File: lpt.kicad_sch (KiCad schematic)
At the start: 25 parts, among them J6 DB25 FEMALE, K1 TE_OJS_5V_10A, Q3 BC857, U2 74HC245, U3 74HC245, U4 LM358EDR2G, U5 ACSL-6400, U7 ACSL-6400

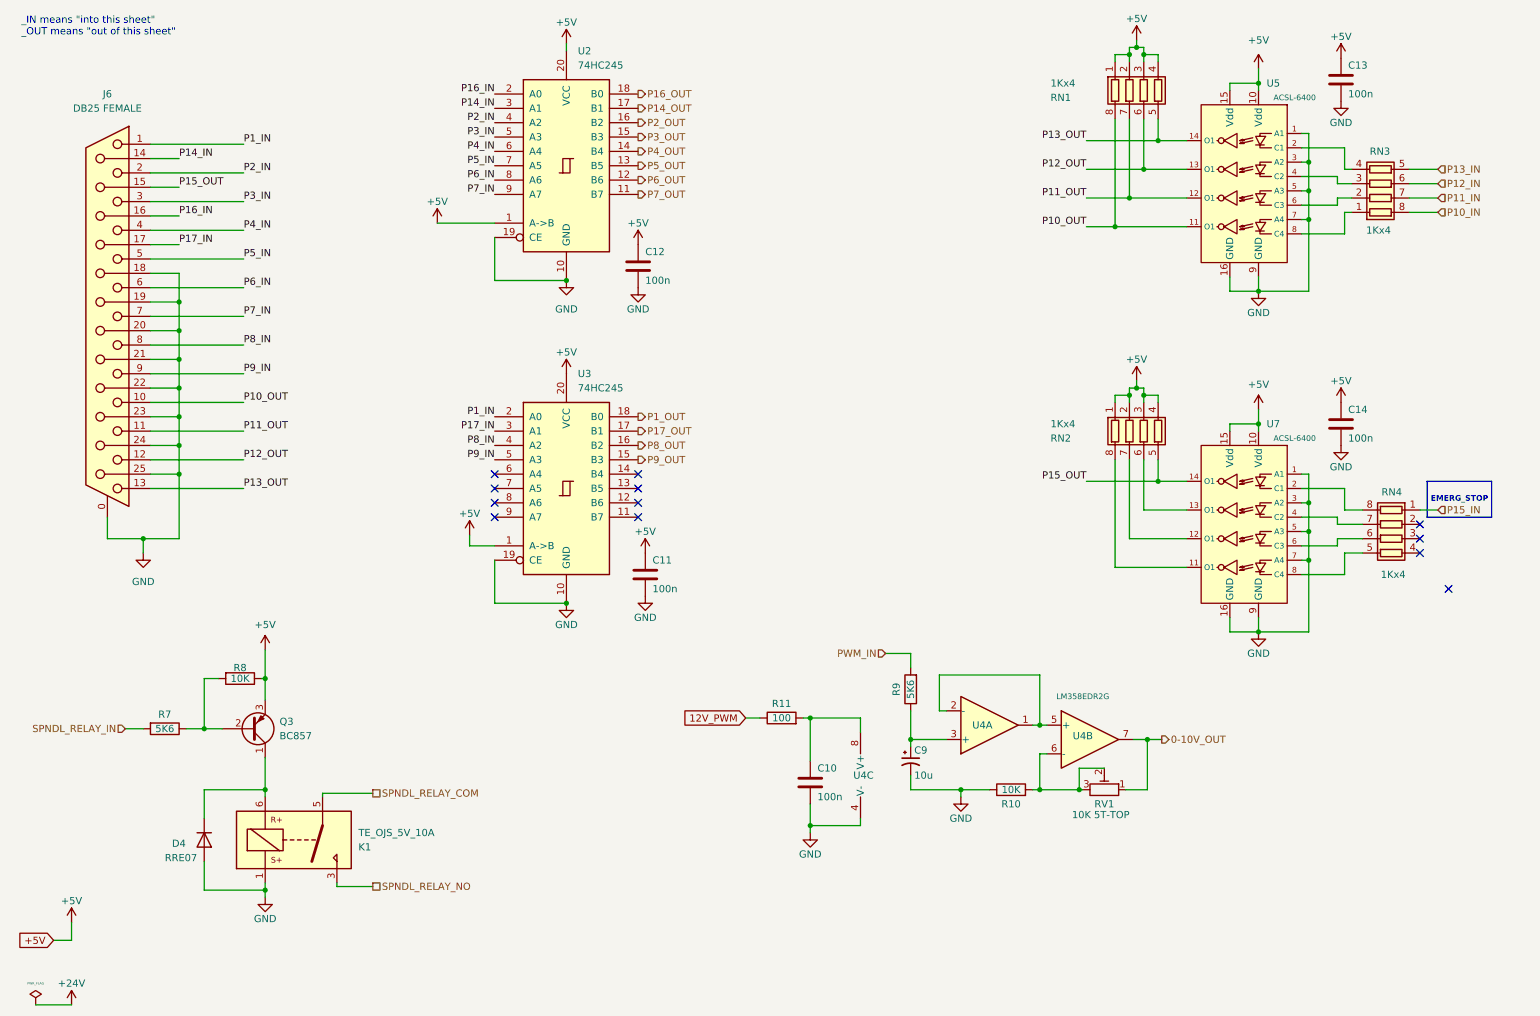
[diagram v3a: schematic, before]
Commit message: Added LEDs (more coming). Changes to charge pump and related power switching.
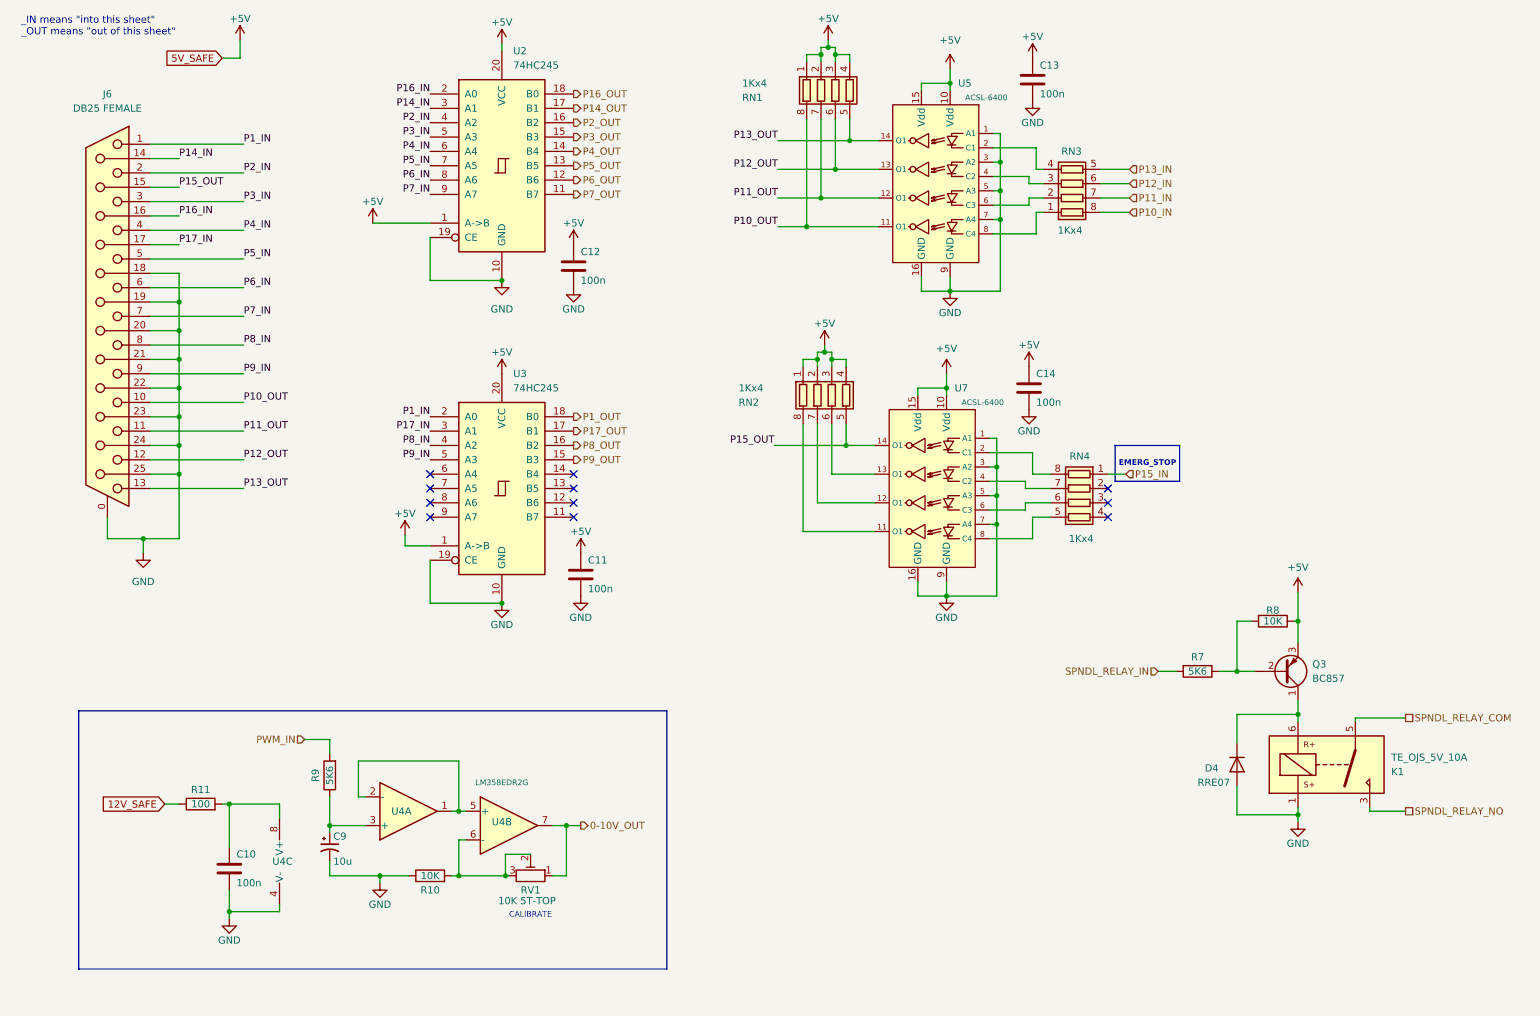
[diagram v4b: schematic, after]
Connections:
- net 12V_PWM renamed 12V_SAFE
- no-connect marks 12 -> 11
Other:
- note added: "CALIBRATE"
- moved on the sheet: C10, C11, C12, C13, C14, C9, D4, K1, Q3, R10, R11, R7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

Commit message: Forgot R1 and more NT fun.
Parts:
- R11: value 100 -> (none)
- U5: value ACSL-6400 -> (none); footprint Package_SO:SO-16_3.9x9.9mm_P1.27mm -> (none)
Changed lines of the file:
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@@
   (no_connect (at 114.3 99.06))
   (no_connect (at 114.3 104.14))
+  (wire (pts (xy 53.34 152.4) (xy 53.34 154.94))
+    (stroke (width 0) (type default) (color 0 0 0 0))
+  )
   (wire (pts (xy 261.62 139.7) (xy 252.73 139.7))
     (stroke (width 0) (type default) (color 0 0 0 0))
@@
     (stroke (width 0) (type default) (color 0 0 0 0))
   )
-  (wire (pts (xy 55.245 22.86) (xy 55.245 19.685))
-    (stroke (width 0) (type default) (color 0 0 0 0))
-  )
   (wire (pts (xy 62.23 173.99) (xy 53.34 173.99))
     (stroke (width 0) (type default) (color 0 0 0 0))
@@
   )
   (wire (pts (xy 154.94 106.68) (xy 167.64 106.68))
-    (stroke (width 0) (type default) (color 0 0 0 0))
-  )
-  (wire (pts (xy 52.07 22.86) (xy 55.245 22.86))
     (stroke (width 0) (type default) (color 0 0 0 0))
   )
@@
     (effects (font (size 1.27 1.27)) (justify right))
     (property "Intersheet References" "${INTERSHEET_REFS}" (id 0) (at 30.4859 154.8606 0)
-      (effects (font (size 1.27 1.27)) (justify right) hide)
-    )
-  )
-  (global_label "5V_SAFE" (shape input) (at 52.07 22.86 180) (fields_autoplaced)
-    (effects (font (size 1.27 1.27)) (justify right))
-    (property "Intersheet References" "${INTERSHEET_REFS}" (id 0) (at 41.8555 22.7806 0)
       (effects (font (size 1.27 1.27)) (justify right) hide)
     )
@@
     )
     (property "Datasheet" "" (id 3) (at 101.6 119.38 0)
+      (effects (font (size 1.27 1.27)) hide)
+    )
+    (pin "1")
+  )
+  (symbol (lib_id "power:PWR_FLAG") (at 53.34 152.4 0) (unit 1)
+    (in_bom yes) (on_board yes) (fields_autoplaced)
+    (property "Reference" "#FLG0103" (id 0) (at 53.34 150.495 0)
+      (effects (font (size 1.27 1.27)) hide)
+    )
+    (property "Value" "PWR_FLAG" (id 1) (at 53.34 147.32 0)
+      (effects (font (size 1.27 1.27)) hide)
+    )
+    (property "Footprint" "" (id 2) (at 53.34 152.4 0)
+      (effects (font (size 1.27 1.27)) hide)
+    )
+    (property "Datasheet" "~" (id 3) (at 53.34 152.4 0)
       (effects (font (size 1.27 1.27)) hide)
     )
@@
     (in_bom yes) (on_board yes)
     (property "Reference" "R11" (id 0) (at 48.26 152.4 90))
-    (property "Value" "100" (id 1) (at 48.26 154.94 90))
+    (property "Value" "" (id 1) (at 48.26 154.94 90))
     (property "Footprint" "Resistor_SMD:R_0603_1608Metric" (id 2) (at 48.26 156.718 90)
       (effects (font (size 1.27 1.27)) hide)
@@
     (pin "1")
     (pin "2")
-  )
-  (symbol (lib_id "power:+5V") (at 55.245 19.685 0) (unit 1)
-    (in_bom yes) (on_board yes)
-    (property "Reference" "#PWR06" (id 0) (at 55.245 23.495 0)
-      (effects (font (size 1.27 1.27)) hide)
-    )
-    (property "Value" "+5V" (id 1) (at 55.245 15.875 0))
-    (property "Footprint" "" (id 2) (at 55.245 19.685 0)
-      (effects (font (size 1.27 1.27)) hide)
-    )
-    (property "Datasheet" "" (id 3) (at 55.245 19.685 0)
-      (effects (font (size 1.27 1.27)) hide)
-    )
-    (pin "1")
   )
   (symbol (lib_id "power:+5V") (at 242.57 117.475 0) (unit 1)
@@
     (pin "1")
   )
-  (symbol (lib_name "ACSL-6400_1") (lib_id "3rd-party:ACSL-6400") (at 178.435 45.085 0) (mirror y) (unit 1)
+  (symbol (lib_id "3rd-party:ACSL-6400") (at 178.435 45.085 0) (mirror y) (unit 1)
     (in_bom yes) (on_board yes)
     (property "Reference" "U5" (id 0) (at 184.785 27.305 0)
       (effects (font (size 1.27 1.27)) (justify left))
     )
-    (property "Value" "ACSL-6400" (id 1) (at 191.135 29.845 0)
+    (property "Value" "" (id 1) (at 191.135 29.845 0)
       (effects (font (size 1 1)) (justify left))
     )
-    (property "Footprint" "Package_SO:SO-16_3.9x9.9mm_P1.27mm" (id 2) (at 178.181 47.625 0)
-      (effects (font (size 1.27 1.27)) hide)
-    )
+    (property "Footprint" "" (id 2) (at 178.181 47.625 0)
+      (effects (font (size 1.27 1.27)) hide)
+    )

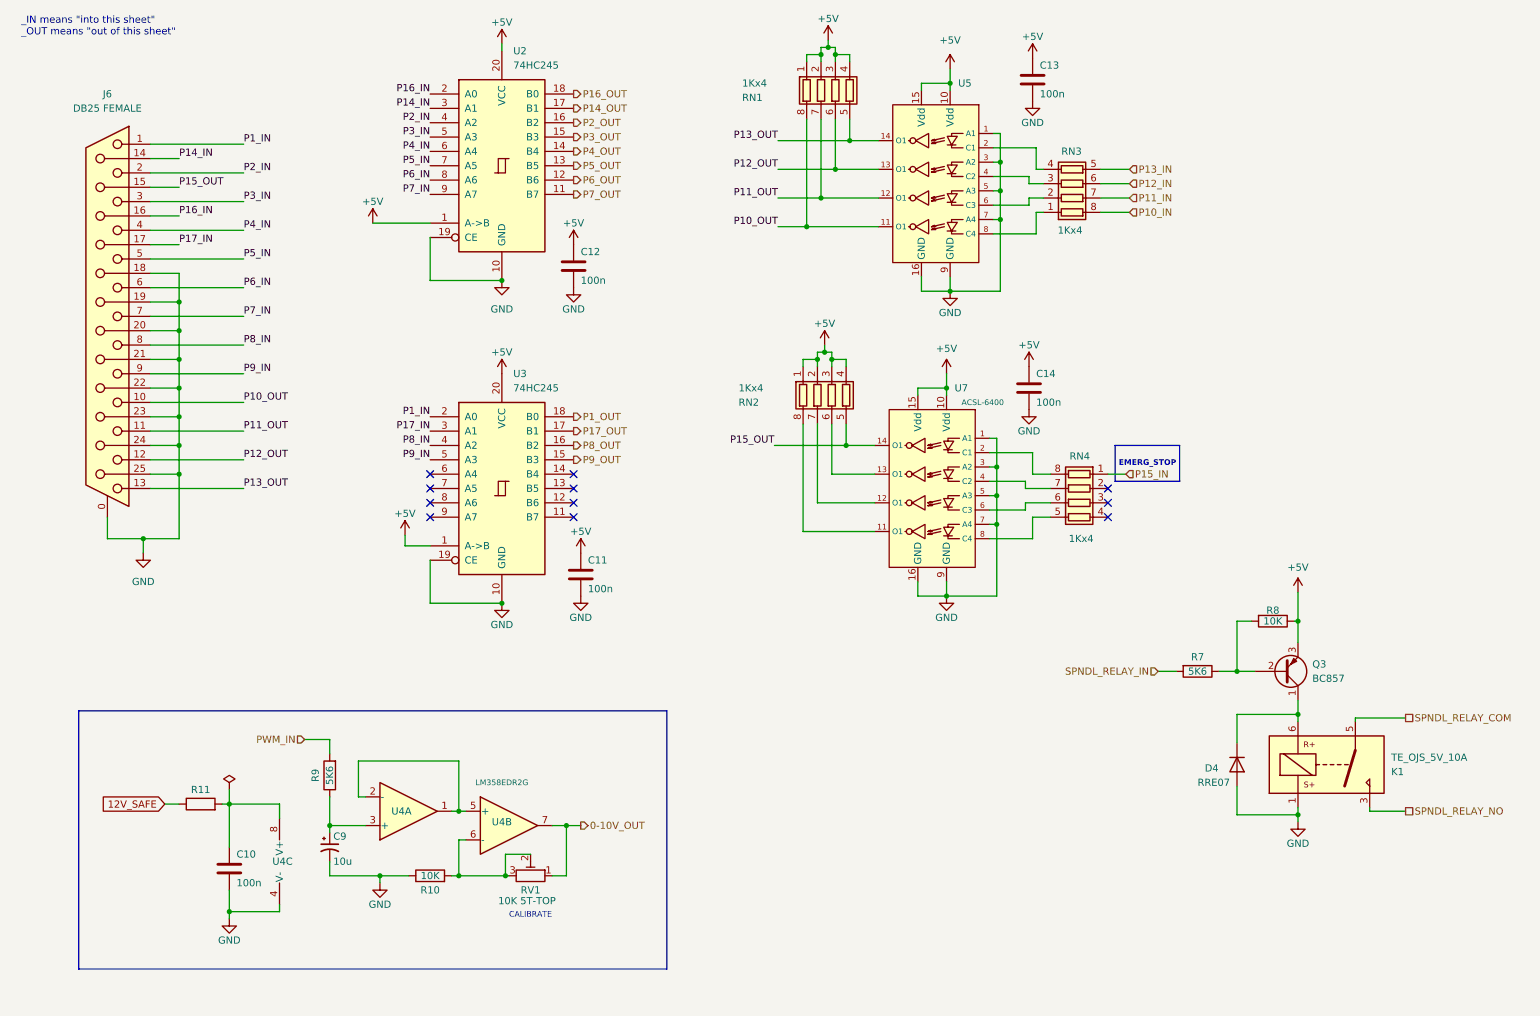
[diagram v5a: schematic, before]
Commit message: Resistor networks changed to 0603 'cause JLCPCB has those as 'basic parts' & aunch of tweaks. (WIP)
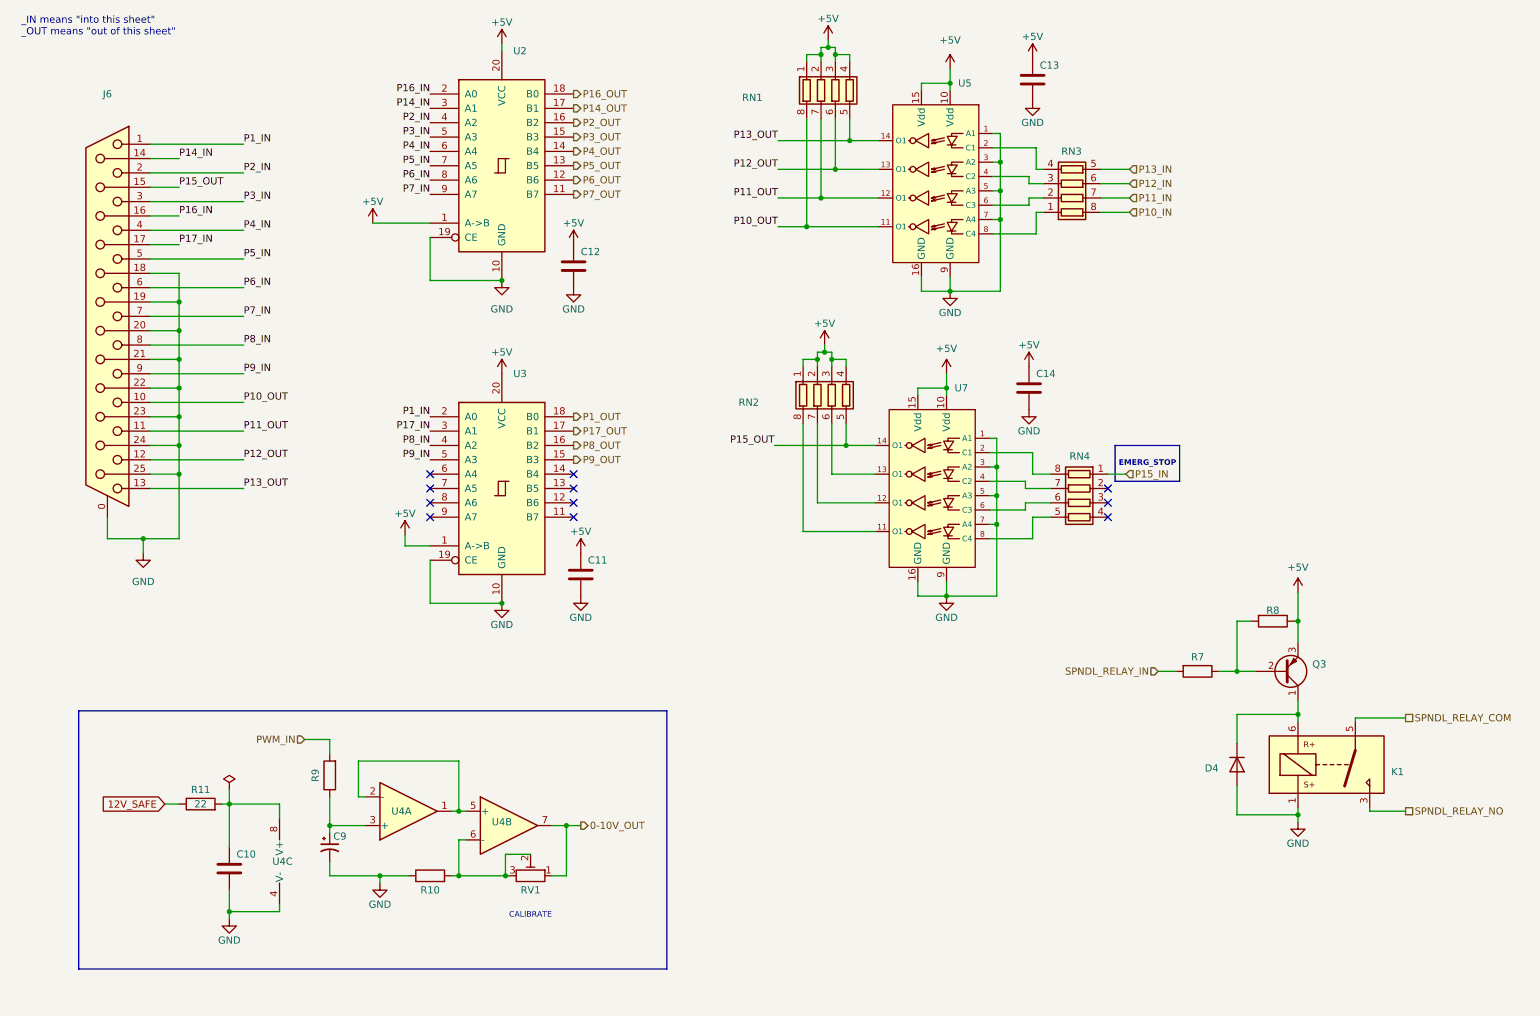
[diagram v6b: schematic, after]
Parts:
- C10, C11, C12, C13, C14: value 100n -> (none); footprint Capacitor_SMD:C_0603_1608Metric -> (none)
- C9: value 10u -> (none); footprint Capacitor_SMD:C_0603_1608Metric -> (none)
- D4: value RRE07 -> (none); footprint Diode_SMD:D_SOD-323_HandSoldering -> (none)
- J6: value DB25 FEMALE -> (none); footprint Connector_Dsub:DSUB-25_Male_Horizontal_P2.77x2.84mm_EdgePinOffset7.70mm_Housed_MountingHolesOffset9.12mm -> (none)
- K1: value TE_OJS_5V_10A -> (none); footprint _footprints:Relay_SPST_ OJS_5V_10A -> (none)
- Q3: value BC857 -> (none); footprint Package_TO_SOT_SMD:SOT-23 -> (none)
- R10, R8: value 10K -> (none); footprint Resistor_SMD:R_0603_1608Metric -> (none)
- R11: value (none) -> 22; footprint Resistor_SMD:R_0603_1608Metric -> (none)
- R7, R9: value 5K6 -> (none); footprint Resistor_SMD:R_0603_1608Metric -> (none)
- RN1, RN2, RN3, RN4: value 1Kx4 -> (none); footprint Resistor_SMD:R_Array_Convex_4x1206 -> (none); Element14 1768299 -> (none); JLCPCB (none) -> C20197; M.Part# (none) -> 4D03WGJ0102T5E; MOQ (none) -> 1
- RV1: value 10K 5T-TOP -> (none); footprint Potentiometer_SMD:Potentiometer_Bourns_3214W_Vertical -> (none)
- U2, U3: value 74HC245 -> (none); footprint Package_SO:SOIC-20W_7.5x12.8mm_P1.27mm -> (none)
- U4: value LM358EDR2G -> (none); footprint Package_SO:SOIC-8_3.9x4.9mm_P1.27mm -> (none)
- U7: value ACSL-6400 -> (none); footprint Package_SO:SO-16_3.9x9.9mm_P1.27mm -> (none)

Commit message: temp
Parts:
- C10, C11, C12, C13, C14: value (none) -> 100n
- C9: value (none) -> 10u
- D4: value (none) -> RRE07; Element14 3407110 -> (none)
- J6: value (none) -> DB25 FEMALE; E14PART (none) -> 1848370; Element14 1848370 -> (none)
- K1: value (none) -> TE_OJS_5V_10A; E14PART (none) -> 3764761; Element14 3764761 -> (none)
- Q3: value (none) -> BC857
- R10, R8: value (none) -> 10K; E14PART (none) -> 2447230; Element14 2447230 -> (none)
- R7, R9: value (none) -> 5K6; E14PART (none) -> 2073537; Element14 2073537 -> (none)
- RN1, RN2, RN3, RN4: value (none) -> 1Kx4; JLCMFR# (none) -> 4D03WGJ0102T5E; JLCPART (none) -> C20197; JLCPCB C20197 -> (none); M.Part# 4D03WGJ0102T5E -> (none)
- RV1: value (none) -> 10K 5T-TOP; E14PART (none) -> 988273; Element14 988273 -> (none)
- U2: value (none) -> 74HC245; E14PART (none) -> 1013973; Element14 1013973 -> (none)
- U3: E14PART (none) -> 1013973; Element14 1013973 -> (none)
- U4: value (none) -> LM358EDR2G; E14PART (none) -> 2844921; Element14 2844921 -> (none)
- U5, U7: value (none) -> ACSL-6400; E14PART (none) -> 9130152; Element14 9130152 -> (none)
